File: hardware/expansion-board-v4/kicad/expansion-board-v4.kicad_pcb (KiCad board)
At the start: 6 copper layers, 100 x 62 mm, 174 parts, among them J1 PinHeader_2x20_P2.54mm_Vertic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, J2 U.FL_Hirose_U.FL-R-SMT-1_Vert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, J4 USB_C_Receptacle_HRO_TYPE-C-3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, J5 U.FL_Hirose_U.FL-R-SMT-1_Vert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, J6 U.FL_Hirose_U.FL-R-SMT-1_Vert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, J7 U.FL_Hirose_U.FL-R-SMT-1_Vert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, J8 U.FL_Hirose_U.FL-R-SMT-1_Vert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, J9 MX1.25WT-2P, Q2 SOT-23, Q3 SOT-23, Q4 SOT-23, Q5 SOT-23, SW2 SolderJumper-2_P1.3mm_Open_Pa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, U1 SOT-23-5, U10 QFN-48-1EP_7x7mm_P0.5mm_EP5.1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, U11 DFN-8-1EP_2x2mm_P0.5mm_EP0.86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, U12 SOT-363_SC-70-6, U13 AD8319_LFCSP-8-EP, U14 MSOP-8_3x3mm_P0.65mm, U15 SOT-23-6, U16 SOT-363_SC-70-6, U17 SOT-363_SC-70-6, U18 SOIC-10_3.9x4.9mm_P1mm, U19 QFN-24-1EP_4x4mm_P0.5mm_EP2.6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, U2 SOT-23-5, U20 TSOT-23-6, U3 SOT-23-5, U4 BNO085_LGA-28, U5 BMP388_LGA-10, U6 LGA-16_3x3mm_P0.5mm, U7 ATGM336H_LCC-18, U8 QFN-56-1EP_7x7mm_P0.4mm_EP3.2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, U9 SOIC-8_5.3x5.3mm_P1.27mm, Y1 Crystal_SMD_3225-4Pin_3.2x2.5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, Y2 Crystal_SMD_3225-4Pin_3.2x2.5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, Y3 Crystal_SMD_3215-2Pin_3.2x1.5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

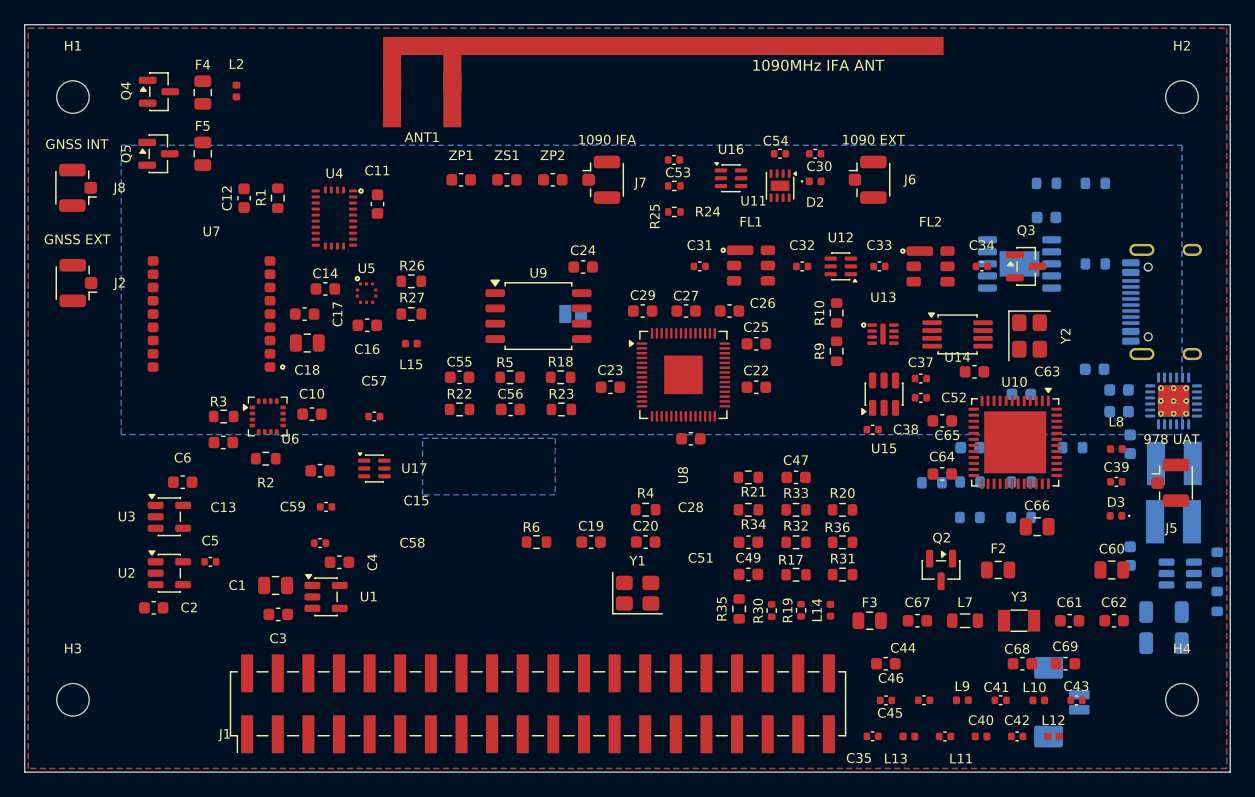
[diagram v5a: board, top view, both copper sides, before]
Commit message: feat(hw): 实现「单面可用」——J4 移 F 面、补 CC 下拉、电源电容改封装
## 单面可用是保底

不带电源版的 B 面现在**零贴装件**，可以走嘉立创经济型单面（¥267.1），
不必被迫上标准型双面（¥614.96）。上一版把 J4 留在 B 面，等于不带电源版
还是双面，只省 ¥35，白做。

三个改动：

  J4 (USB-C) → F 面 (144.63,73.00) rot=0
      courtyard 右沿贴齐板边 150，开口仍朝 +X（与微雪 H1 同侧）。
      翻面会镜像 x 且 USB-C 封装原点不在几何中心，x 是重新解出来的。
      USB_DP/DM 连的 R9/R10 本来就在 F 面 x117，搬过去走线反而更短；
      USB_CC1/2 与 USB_VBUS 只有带电源版才用，跨面过孔即可。

  新增 R7/R8（5.1k CC 下拉）→ F 面，紧邻 J4 2.2mm
      不带电源版没有 CH224K，CC 悬空则主机根本不认设备——USB-C 规范要求
      device 端呈现 Rd 才会被检测和枚举，不枚举就没法 UF2 刷机。
      **与 CH224K 二选一**，带电源版不贴。

  R37 (138.80,69.84) → (137.75,70.75)
      J4 的通孔安装脚穿到 B 面，落进了 R37 的 courtyard（DRC 报
      pth_inside_courtyard）。顺带把它到 CH224K CFG1 脚的距离 2.97→2.56mm。

## 电源电容改封装

不是为散热——电阻功率算过，最大的 R43 也才 (9−3.3)²/1k = 32.5mW，
0603 有 3 倍余量。真正的理由是两条：

  C72  6.8µF/25V  0603 → 1206
      接 PD 诱骗后的 9V 侧，耐压不能降。而 0603 在 25V 档容值上限只有
      1~2.2µF，6.8µF/25V 根本买不到。换封装后原位撞 C80，已就近重贴
      （按「离同网芯片引脚最近」而不是「离原位最近」找的位）。

  C73/C74/C75  10µF  0603 → 0805
      直流偏置下的容值衰减：10µF/16V X5R 在 5V 偏压下，0603 只剩
      3~4µF(−60%)，0805 还有 6~7µF(−30%)，直接影响输出纹波。

## 新增电源采购 CSV（单独一份，不混进整板 xlsx）

tools/gen_power_csv.py → BOM_电源采购_淘宝.csv，22 种料 / 30 颗。
按「卖家怎么找货」分组，同规格合并给总数，备注写清耐压/精度/为什么
封装不能换，末尾附两个版本的贴装差异。整板 88 料号的 xlsx 发给卖家太乱。

验收：DRC error 0 条，F 面丝印全通过，原理图↔PCB 零不一致，
176 元件已固化，全套文档重生成（BOM 88 料号 / SMT 79 料号 164 贴片位）。
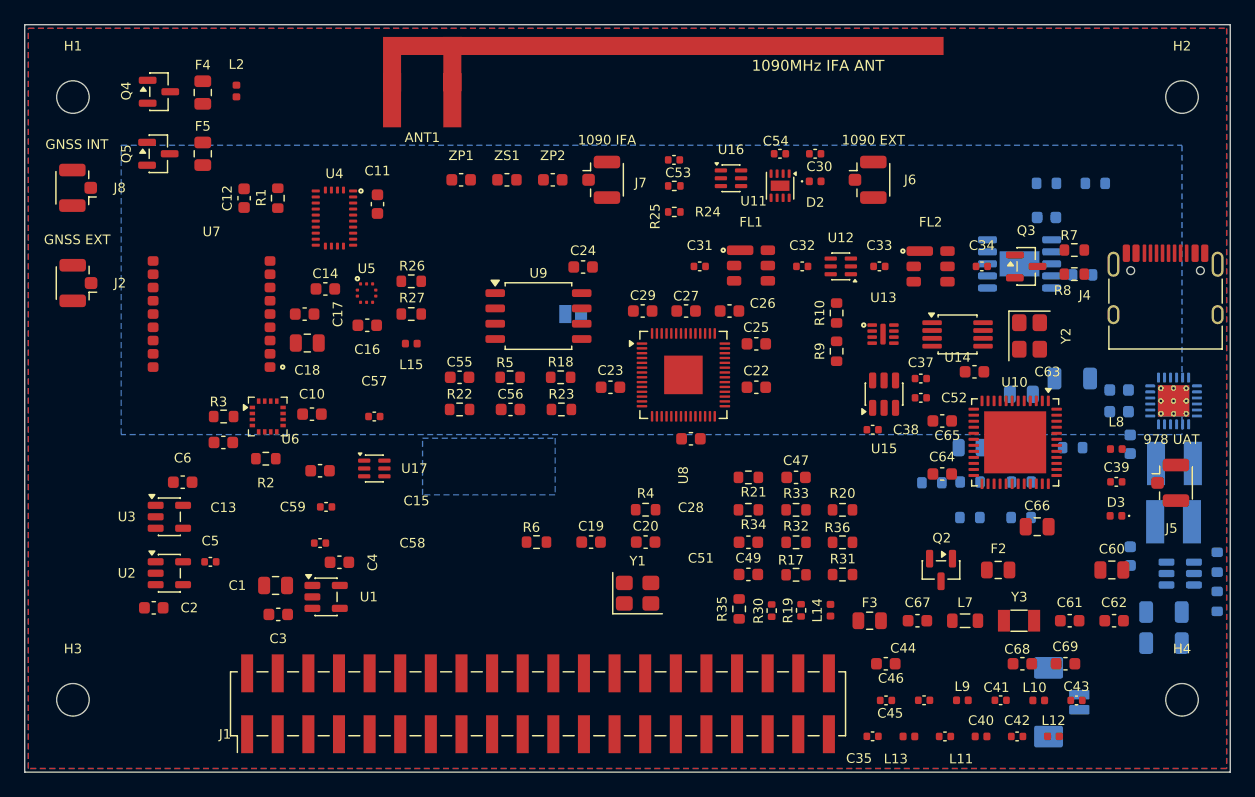
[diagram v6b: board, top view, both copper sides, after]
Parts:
- added R7: 5.1k, R_0603_1608Metric, F.Cu at (137.1, 68.7)
- added R8: 5.1k, R_0603_1608Metric, F.Cu at (137.1, 70.7)
- C72: footprint C_0603_1608Metric -> C_1206_3216Metric
- C73, C74, C75: footprint C_0603_1608Metric -> C_0805_2012Metric
- J4: moved to F.Cu
- moved C72 2.00 mm to (136.9, 79.3)
- moved R37 1.39 mm to (137.8, 70.8)
- moved J4 1.17 mm to (144.6, 73.0), turned to 0 degrees

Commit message: fix(hw): J4 开口方向判错（朝板内），改 rot=90；变体选贴加丝印框+文档
## J4 朝向是错的，用户指出后查实

我上一版选了 rot=0，判据是「焊盘重心在 courtyard 中心左侧 = 开口朝右」。
这个判据从根上就不成立：

    rot=  0  courtyard 10.73 x 9.51  长轴x  焊盘重心(144.63,69.63) vs 中心(144.63,72.44)
    → 长轴在 x 时焊盘正好沿 x 展开，重心 ≈ 中心，pad_cx 与中心比大小的结果是随机的

USB-C 卧贴座的插口在**焊盘的反方向**，而插口宽度方向就是 courtyard 的长边，
所以开口只能垂直于长轴。rot=0 时长轴在 x，开口朝 +y——**朝板内，根本插不了线**。

正确判据要先看长轴：长轴在 y 才可能朝 ±x，再用焊盘重心定左右。
改 rot=90 后解出 (145.81, 73.00)，courtyard x140.49~150.00，右沿贴齐板边，
开口朝 +x；VBUS 焊盘落在 x141.76（朝板内），过孔就近打不必绕本体；
到 J5(978 U.FL) 还有 7.09mm。判据已写回 apply_single_side.py。

## 变体选贴：加丝印框 + 写进装配文档

「B 面不贴时 F 面才贴」是反向逻辑，光靠 BOM 备注挡不住装配出错。

  · gen_silk.py 新增 VARIANT_BOX：给 R7/R8 画丝印框 + 标注 NO-PWR VER。
    标注放框**上方**（下方 1mm 处紧邻 Y2 的 courtyard），文案也缩短过——
    15 字符的 NO-PWR VER ONLY 会伸到 J4 底下。
    清理旧标注按**前缀**匹配：按完整文字匹配的话，改一次文案就清不掉旧的，
    实测新旧两条并存。
  · ASSEMBLY.md 开头加「装配前先确认做哪个版本」表格，讲清为什么是反的：
    带电源版 CH224K 内部提供 Rd，此时外挂 R7/R8 会让 CC 阻值错乱干扰 PD；
    不带电源版不贴 R7/R8 则 CC 悬空，插上电脑毫无反应、刷不了固件。
  · CHECKLIST.md 加同样的指引。两份都是改生成脚本模板，不是改产物。

验收：DRC error 0 条，F 面丝印全通过，176 元件已固化，
全套文档重生成（ASSEMBLY 164 件 / CHECKLIST 176 位号 / BOM 88 料号 /
SMT 79 料号 164 贴片位 / 电源采购 CSV 22 种料）。
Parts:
- moved J4 1.17 mm to (145.8, 73.0), turned to 90 degrees
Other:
- board text added: "NO-PWR VER"
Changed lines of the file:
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@@
 				(font
 					(size 0.8 0.8)
-					(thickness 0.136)
+					(thickness 0.15)
 				)
 			)
@@
 				(font
 					(size 0.8 0.8)
-					(thickness 0.136)
+					(thickness 0.15)
 				)
 			)
@@
 	(footprint "USB_C_Receptacle_HRO_TYPE-C-31-M-12"
 		(layer "F.Cu")
-		(at 144.635 73)
+		(at 145.805 73 90)
 		(descr "USB Type-C receptacle for USB 2.0 and PD, http://www.krhro.com/uploads/soft/180320/1-1P320120243.pdf")
 		(tags "usb usb-c 2.0 pd")
 		(property "Reference" "J4"
-			(at -6.696 -0.56 0)
+			(at 0.56 -7.866 0)
 			(layer "F.SilkS")
 			(effects
@@
 		)
 		(property "Value" "USB_C_Receptacle_HRO_TYPE-C-31-M-12"
-			(at 0 5.1 180)
+			(at 0 5.1 270)
 			(layer "F.Fab")
 			(effects
@@
 		)
 		(property "Datasheet" ""
-			(at 0 0 0)
+			(at 0 0 90)
 			(unlocked yes)
 			(layer "F.Fab")
@@
 		)
 		(property "Description" ""
-			(at 0 0 0)
+			(at 0 0 90)
 			(unlocked yes)
 			(layer "F.Fab")
@@
 		(duplicate_pad_numbers_are_jumpers no)
 		(fp_line
-			(start -4.7 -1.9)
-			(end -4.7 0.1)
+			(start 4.7 -1.9)
+			(end 4.7 0.1)
 			(stroke
 				(width 0.12)
@@
 		)
 		(fp_line
-			(start -4.7 2)
-			(end -4.7 3.9)
+			(start -4.7 -1.9)
+			(end -4.7 0.1)
 			(stroke
 				(width 0.12)
@@
 		)
 		(fp_line
-			(start -4.7 3.9)
+			(start 4.7 2)
 			(end 4.7 3.9)
 			(stroke
@@
 		)
 		(fp_line
-			(start 4.7 -1.9)
-			(end 4.7 0.1)
+			(start -4.7 2)
+			(end -4.7 3.9)
 			(stroke
 				(width 0.12)
@@
 		)
 		(fp_line
-			(start 4.7 2)
+			(start -4.7 3.9)
 			(end 4.7 3.9)
 			(stroke
@@
 		)
 		(fp_line
-			(start -5.32 -5.27)
-			(end -5.32 4.15)
+			(start 5.32 -5.27)
+			(end 5.32 4.15)
 			(stroke
 				(width 0.05)
@@
 		)
 		(fp_line
-			(start -5.32 4.15)
-			(end 5.32 4.15)
+			(start -5.32 -5.27)
+			(end -5.32 4.15)
 			(stroke
 				(width 0.05)
@@
 		)
 		(fp_line
-			(start 5.32 -5.27)
+			(start -5.32 4.15)
 			(end 5.32 4.15)
 			(stroke
@@
 		)
 		(fp_line
-			(start -4.47 -3.65)
-			(end -4.47 3.65)
+			(start 4.47 -3.65)
+			(end 4.47 3.65)
 			(stroke
 				(width 0.1)
@@
 		)
 		(fp_line
-			(start -4.47 3.65)
-			(end 4.47 3.65)
+			(start -4.47 -3.65)
+			(end -4.47 3.65)
 			(stroke
 				(width 0.1)
@@
 		)
 		(fp_line
-			(start 4.47 -3.65)
+			(start -4.47 3.65)
 			(end 4.47 3.65)
 			(stroke
@@
 		)
 		(fp_text user "${REFERENCE}"
-			(at 0 0 180)
+			(at 0 0 270)
 			(layer "F.Fab")
 			(effects
@@
 		)
 		(pad "" np_thru_hole circle
-			(at -2.89 -2.6)
+			(at -2.89 -2.6 90)
 			(size 0.65 0.65)
 			(drill 0.65)
@@
 		)
 		(pad "" np_thru_hole circle
-			(at 2.89 -2.6)
+			(at 2.89 -2.6 90)
 			(size 0.65 0.65)
 			(drill 0.65)
@@
 		)
 		(pad "A1" smd roundrect
-			(at -3.25 -4.045)
+			(at -3.25 -4.045 90)
 			(size 0.6 1.45)
 			(layers "F.Cu" "F.Mask" "F.Paste")
@@
 		)
 		(pad "A4" smd roundrect
-			(at -2.45 -4.045)
+			(at -2.45 -4.045 90)
 			(size 0.6 1.45)
 			(layers "F.Cu" "F.Mask" "F.Paste")
@@
 		)
 		(pad "A5" smd roundrect
-			(at -1.25 -4.045)
+			(at -1.25 -4.045 90)
 			(size 0.3 1.45)
 			(layers "F.Cu" "F.Mask" "F.Paste")
@@
 		)
 		(pad "A6" smd roundrect
-			(at -0.25 -4.045)
+			(at -0.25 -4.045 90)
 			(size 0.3 1.45)
 			(layers "F.Cu" "F.Mask" "F.Paste")
@@
 		)
 		(pad "A7" smd roundrect
-			(at 0.25 -4.045)
+			(at 0.25 -4.045 90)
 			(size 0.3 1.45)
 			(layers "F.Cu" "F.Mask" "F.Paste")
@@
 		)
 		(pad "A8" smd roundrect
-			(at 1.25 -4.045)
+			(at 1.25 -4.045 90)
 			(size 0.3 1.45)
 			(layers "F.Cu" "F.Mask" "F.Paste")
@@
 		)
 		(pad "A9" smd roundrect
-			(at 2.45 -4.045)
+			(at 2.45 -4.045 90)
 			(size 0.6 1.45)
 			(layers "F.Cu" "F.Mask" "F.Paste")
@@
 		)
 		(pad "A12" smd roundrect
-			(at 3.25 -4.045)
+			(at 3.25 -4.045 90)
 			(size 0.6 1.45)
 			(layers "F.Cu" "F.Mask" "F.Paste")
@@
 		)
 		(pad "B1" smd roundrect
-			(at 3.25 -4.045)
+			(at 3.25 -4.045 90)
 			(size 0.6 1.45)
 			(layers "F.Cu" "F.Mask" "F.Paste")
@@
 		)
 		(pad "B4" smd roundrect
-			(at 2.45 -4.045)
+			(at 2.45 -4.045 90)
 			(size 0.6 1.45)
 			(layers "F.Cu" "F.Mask" "F.Paste")
@@
 		)
 		(pad "B5" smd roundrect
-			(at 1.75 -4.045)
+			(at 1.75 -4.045 90)
 			(size 0.3 1.45)
 			(layers "F.Cu" "F.Mask" "F.Paste")
@@
 		)
 		(pad "B6" smd roundrect
-			(at 0.75 -4.045)
+			(at 0.75 -4.045 90)
 			(size 0.3 1.45)
 			(layers "F.Cu" "F.Mask" "F.Paste")
@@
 		)
 		(pad "B7" smd roundrect
-			(at -0.75 -4.045)
+			(at -0.75 -4.045 90)
 			(size 0.3 1.45)
 			(layers "F.Cu" "F.Mask" "F.Paste")
@@
 		)
 		(pad "B8" smd roundrect
-			(at -1.75 -4.045)
+			(at -1.75 -4.045 90)
 			(size 0.3 1.45)
 			(layers "F.Cu" "F.Mask" "F.Paste")
@@
 		)
 		(pad "B9" smd roundrect
-			(at -2.45 -4.045)
+			(at -2.45 -4.045 90)
 			(size 0.6 1.45)
 			(layers "F.Cu" "F.Mask" "F.Paste")
@@
 		)
 		(pad "B12" smd roundrect
-			(at -3.25 -4.045)
+			(at -3.25 -4.045 90)
 			(size 0.6 1.45)
 			(layers "F.Cu" "F.Mask" "F.Paste")
@@
 		)
 		(pad "SH" thru_hole oval
-			(at -4.32 -3.13)
+			(at -4.32 -3.13 90)
 			(size 1 2.1)
 			(drill oval 0.6 1.7)
@@
 		)
 		(pad "SH" thru_hole oval
-			(at -4.32 1.05)
+			(at -4.32 1.05 90)
 			(size 1 1.6)
 			(drill oval 0.6 1.2)
@@
 		)
 		(pad "SH" thru_hole oval
-			(at 4.32 -3.13)
+			(at 4.32 -3.13 90)
 			(size 1 2.1)
 			(drill oval 0.6 1.7)
@@
 		)
 		(pad "SH" thru_hole oval
-			(at 4.32 1.05)
+			(at 4.32 1.05 90)
 			(size 1 1.6)
 			(drill oval 0.6 1.2)
@@
 				(font
 					(size 0.8 0.8)
-					(thickness 0.136)
+					(thickness 0.15)
 				)
 				(justify mirror)
@@
 				(font
 					(size 0.8 0.8)
-					(thickness 0.136)
+					(thickness 0.15)
 				)
 				(justify mirror)
@@
 				(font
 					(size 0.8 0.8)
-					(thickness 0.136)
+					(thickness 0.15)
 				)
 				(justify mirror)
@@
 				(font
 					(size 0.8 0.8)
-					(thickness 0.136)
+					(thickness 0.15)
 				)
 				(justify mirror)
@@
 				(font
 					(size 0.8 0.8)
-					(thickness 0.136)
+					(thickness 0.15)
 				)
 				(justify mirror)
@@
 				(font
 					(size 0.8 0.8)
-					(thickness 0.136)
+					(thickness 0.15)
 				)
 				(justify mirror)
@@
 	)
 	(gr_line
+		(start 135.095 67.465)
+		(end 139.045 67.465)
+		(stroke
+			(width 0.15)
+			(type default)
+		)
+		(layer "F.SilkS")
+	)
+	(gr_line
+		(start 135.095 71.915)
+		(end 135.095 67.465)
+		(stroke
+			(width 0.15)
+			(type default)
+		)
+		(layer "F.SilkS")
+	)
+	(gr_line
+		(start 139.045 67.465)
+		(end 139.045 71.915)
+		(stroke
+			(width 0.15)
+			(type default)
+		)
+		(layer "F.SilkS")
+	)
+	(gr_line
+		(start 139.045 71.915)
+		(end 135.095 71.915)
+		(stroke
+			(width 0.15)
+			(type default)
+		)
+		(layer "F.SilkS")
+	)
+	(gr_line
 		(start 50 50)
 		(end 150 50)
@@
 		(layer "Edge.Cuts")
 	)
+	(gr_text "NO-PWR VER"
+		(at 137.07 66.465 0)
+		(layer "F.SilkS")
+		(effects
+			(font
+				(size 0.7 0.7)
+				(thickness 0.12)
+			)
+		)
+	)
 	(gr_text "GNSS INT"

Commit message: chore(hw): 固化人工调整的 R7/R8/RT1 位置，全套文档重生成
人工在 KiCad 里调了三个件（相对上次固化）：

  R7   F面 (137.07,68.69) rot0   → (145.59,64.78) rot270   移动 9.37mm
  R8   F面 (137.07,70.69) rot0   → (143.59,64.78) rot270   移动 8.80mm
  RT1  B面 (125.25,88.00) rot180 → (122.63,87.73) rot90    移动 2.63mm

逐项复核后固化，检查结论：

## 全部通过

  RT1 三个约束           在电池投影区内 ✅ / 离最近发热源 20.4mm ✅（≥15mm 才测得到
                         电池温度而不是板温）/ CHG_NTC 到分压电阻 6.65mm ✅
  SW2 的 QSPI 片选 stub  6.08mm（对比 QSPI_SCLK 全长 7.4mm）✅
  功率回路              11 项里 10 项达标，LX/BST 这些关键项全在 2~4.4mm
  不带电源版 B 面        零贴装件 ✅ 单面目标保持
  变体丝印框            已跟随 R7/R8 到新位置，框住两颗、标注 NO-PWR VER ✅
  DRC error             0 条
  F 面丝印              全部通过

## 三处数字变化，评估后判定可接受，未改动

1. **R7 → J4.CC1 从 8.05mm 变 10.99mm**
   CC 是 PD 协商线，BMC 编码约 300kHz，不是高速信号；规范约束的是
   CC 对地电容 <600pF，11mm 走线才 1~2pF。长度不构成问题。

2. **C72 → U19.CHG_PMID 8.01mm**
   注意：上一版我报的 6.56mm 是**元件中心到引脚**，这次按引脚到引脚重算才是
   真实走线长度，8.01mm 才对，之前那个数偏乐观。
   全区扫描后最优也只有 7.18mm（B 面挤，1206 封装大），改善 0.83mm 不值得
   打乱刚调好的布局。8mm 走线电感约 8nH，1.5MHz 下阻抗 0.075Ω，
   对 PMID 纹波影响很小——它是输入电容，不像 BST/LX 那样敏感。

3. **R37 ↔ U18 courtyard 重叠 0.04mm**
   courtyard 是装配安全边界，0603 的比本体每边大 0.25mm。实测**本体间距
   2.38mm**，没有真碰上，DRC 也没报（courtyard 重叠是 warning 不是 error）。

固化结果：PLACEMENT.py 176 元件 / 176 位号。
文档同步重生成：ASSEMBLY 164 件、CHECKLIST 176 位号、BOM 88 料号、
SMT 79 料号 164 贴片位、电源采购 CSV 22 种料。
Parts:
- moved R7 9.37 mm to (145.6, 64.8), turned to -90 degrees
- moved R8 8.80 mm to (143.6, 64.8), turned to -90 degrees
- moved RT1 2.63 mm to (122.6, 87.7), turned to 90 degrees
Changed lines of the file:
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@@
 	(footprint "R_0603_1608Metric"
 		(layer "F.Cu")
-		(at 137.07 70.69)
+		(at 143.587 64.7762 -90)
 		(descr "Resistor SMD 0603 (1608 Metric), square (rectangular) end terminal, IPC-7351 nominal, (Body size source: IPC-SM-782 page 72, https://www.pcb-3d.com/wordpress/wp-content/uploads/ipc-sm-782a_amendment_1_and_2.pdf)")
 		(tags "resistor")
 		(property "Reference" "R8"
-			(at -0.975 1.353 0)
+			(at 0.0446 1.9058 90)
 			(layer "F.SilkS")
 			(effects
@@
 		)
 		(property "Value" "5.1k"
-			(at 0 1.43 0)
+			(at 0 1.43 90)
 			(layer "F.Fab")
 			(effects
@@
 		)
 		(property "Datasheet" ""
-			(at 0 0 0)
+			(at 0 0 90)
 			(layer "F.Fab")
 			(hide yes)
@@
 		)
 		(property "Description" ""
-			(at 0 0 0)
+			(at 0 0 90)
 			(layer "F.Fab")
 			(hide yes)
@@
 		)
 		(property "KiLib_Generator" "SMD_2terminal_chip_molded"
-			(at 0 0 0)
+			(at 0 0 90)
 			(layer "F.SilkS")
 			(hide yes)
@@
 		(duplicate_pad_numbers_are_jumpers no)
 		(fp_line
-			(start -0.237258 -0.5225)
-			(end 0.237258 -0.5225)
+			(start -0.237258 0.5225)
+			(end 0.237258 0.5225)
 			(stroke
 				(width 0.12)
@@
 		)
 		(fp_line
-			(start -0.237258 0.5225)
-			(end 0.237258 0.5225)
+			(start -0.237258 -0.5225)
+			(end 0.237258 -0.5225)
 			(stroke
 				(width 0.12)
@@
 		)
 		(fp_text user "${REFERENCE}"
-			(at 0 0 0)
+			(at 0 0 90)
 			(layer "F.Fab")
 			(effects
@@
 		)
 		(pad "1" smd roundrect
-			(at -0.825 0)
+			(at -0.825 0 270)
 			(size 0.8 0.95)
 			(layers "F.Cu" "F.Mask" "F.Paste")
@@
 		)
 		(pad "2" smd roundrect
-			(at 0.825 0)
+			(at 0.825 0 270)
 			(size 0.8 0.95)
 			(layers "F.Cu" "F.Mask" "F.Paste")
@@
 	(footprint "R_0603_1608Metric"
 		(layer "F.Cu")
-		(at 137.07 68.69)
+		(at 145.587 64.7762 -90)
 		(descr "Resistor SMD 0603 (1608 Metric), square (rectangular) end terminal, IPC-7351 nominal, (Body size source: IPC-SM-782 page 72, https://www.pcb-3d.com/wordpress/wp-content/uploads/ipc-sm-782a_amendment_1_and_2.pdf)")
 		(tags "resistor")
 		(property "Reference" "R7"
-			(at -0.427 -1.219 0)
+			(at -0.0062 -1.913 90)
 			(layer "F.SilkS")
 			(effects
@@
 		)
 		(property "Value" "5.1k"
-			(at 0 1.43 0)
+			(at 0 1.43 90)
 			(layer "F.Fab")
 			(effects
@@
 		)
 		(property "Datasheet" ""
-			(at 0 0 0)
+			(at 0 0 90)
 			(layer "F.Fab")
 			(hide yes)
@@
 		)
 		(property "Description" ""
-			(at 0 0 0)
+			(at 0 0 90)
 			(layer "F.Fab")
 			(hide yes)
@@
 		)
 		(property "KiLib_Generator" "SMD_2terminal_chip_molded"
-			(at 0 0 0)
+			(at 0 0 90)
 			(layer "F.SilkS")
 			(hide yes)
@@
 		(duplicate_pad_numbers_are_jumpers no)
 		(fp_line
-			(start -0.237258 -0.5225)
-			(end 0.237258 -0.5225)
+			(start -0.237258 0.5225)
+			(end 0.237258 0.5225)
 			(stroke
 				(width 0.12)
@@
 		)
 		(fp_line
-			(start -0.237258 0.5225)
-			(end 0.237258 0.5225)
+			(start -0.237258 -0.5225)
+			(end 0.237258 -0.5225)
 			(stroke
 				(width 0.12)
@@
 		)
 		(fp_text user "${REFERENCE}"
-			(at 0 0 0)
+			(at 0 0 90)
 			(layer "F.Fab")
 			(effects
@@
 		)
 		(pad "1" smd roundrect
-			(at -0.825 0)
+			(at -0.825 0 270)
 			(size 0.8 0.95)
 			(layers "F.Cu" "F.Mask" "F.Paste")
@@
 		)
 		(pad "2" smd roundrect
-			(at 0.825 0)
+			(at 0.825 0 270)
 			(size 0.8 0.95)
 			(layers "F.Cu" "F.Mask" "F.Paste")
@@
 		(tags "usb usb-c 2.0 pd")
 		(property "Reference" "J4"
-			(at 0.56 -7.866 0)
+			(at 0.0512 -6.1304 0)
 			(layer "F.SilkS")
 			(effects
@@
 	(footprint "R_0603_1608Metric"
 		(layer "B.Cu")
-		(at 125.25 88 180)
+		(at 122.6312 87.7316 90)
 		(descr "Resistor SMD 0603 (1608 Metric), square (rectangular) end terminal, IPC-7351 nominal, (Body size source: IPC-SM-782 page 72, https://www.pcb-3d.com/wordpress/wp-content/uploads/ipc-sm-782a_amendment_1_and_2.pdf)")
 		(tags "resistor")
 		(property "Reference" "RT1"
-			(at -0.427 -1.219 0)
+			(at 0.0144 1.3208 90)
 			(layer "B.SilkS")
 			(effects
@@
 		)
 		(property "Value" "NCP18XH103F03RB 10k NTC"
-			(at 0 -1.43 0)
+			(at 0 -1.43 90)
 			(layer "B.Fab")
 			(effects
@@
 		)
 		(property "Datasheet" ""
-			(at 0 0 0)
+			(at 0 0 90)
 			(layer "B.Fab")
 			(hide yes)
@@
 		)
 		(property "Description" ""
-			(at 0 0 0)
+			(at 0 0 90)
 			(layer "B.Fab")
 			(hide yes)
@@
 		)
 		(property "KiLib_Generator" "SMD_2terminal_chip_molded"
-			(at 0 0 0)
+			(at 0 0 90)
 			(layer "B.SilkS")
 			(hide yes)
@@
 		(duplicate_pad_numbers_are_jumpers no)
 		(fp_line
-			(start -0.237258 0.5225)
-			(end 0.237258 0.5225)
+			(start -0.237258 -0.5225)
+			(end 0.237258 -0.5225)
 			(stroke
 				(width 0.12)
@@
 		)
 		(fp_line
-			(start -0.237258 -0.5225)
-			(end 0.237258 -0.5225)
+			(start -0.237258 0.5225)
+			(end 0.237258 0.5225)
 			(stroke
 				(width 0.12)
@@
 		)
 		(fp_text user "${REFERENCE}"
-			(at 0 0 0)
+			(at 0 0 90)
 			(layer "B.Fab")
 			(effects
@@
 		)
 		(pad "1" smd roundrect
-			(at -0.825 0 180)
+			(at -0.825 0 90)
 			(size 0.8 0.95)
 			(layers "B.Cu" "B.Mask" "B.Paste")
@@
 		)
 		(pad "2" smd roundrect
-			(at 0.825 0 180)
+			(at 0.825 0 90)
 			(size 0.8 0.95)
 			(layers "B.Cu" "B.Mask" "B.Paste")
@@
 		(tags "resistor")
 		(property "Reference" "R39"
-			(at -0.427 -1.2198 0)
+			(at -0.0206 -1.2706 0)
 			(layer "B.SilkS")
 			(effects
@@
 		(tags "resistor")
 		(property "Reference" "R40"
-			(at -0.427001 -1.2198 0)
+			(at -0.020601 -1.2706 0)
 			(layer "B.SilkS")
 			(effects
@@
 		(tags "solder jumper open")
 		(property "Reference" "SW2"
-			(at 0.516 1.541 0)
+			(at -0.0468 -1.6608 0)
 			(layer "B.SilkS")
 			(effects
@@
 	)
 	(gr_line
-		(start 135.095 67.465)
-		(end 139.045 67.465)
+		(start 142.362 62.8012)
+		(end 146.812 62.8012)
 		(stroke
 			(width 0.15)
@@
 	)
 	(gr_line
-		(start 135.095 71.915)
-		(end 135.095 67.465)
+		(start 142.362 66.7512)
+		(end 142.362 62.8012)
 		(stroke
 			(width 0.15)
@@
 	)
 	(gr_line
-		(start 139.045 67.465)
-		(end 139.045 71.915)
+		(start 146.812 62.8012)
+		(end 146.812 66.7512)
 		(stroke
 			(width 0.15)
@@
 	)
 	(gr_line
-		(start 139.045 71.915)
-		(end 135.095 71.915)
+		(start 146.812 66.7512)
+		(end 142.362 66.7512)
 		(stroke
 			(width 0.15)
@@
 	)
 	(gr_text "NO-PWR VER"
-		(at 137.07 66.465 0)
+		(at 144.5 62 0)
 		(layer "F.SilkS")
 		(effects
